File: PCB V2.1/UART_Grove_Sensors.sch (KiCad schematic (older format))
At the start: 0 parts

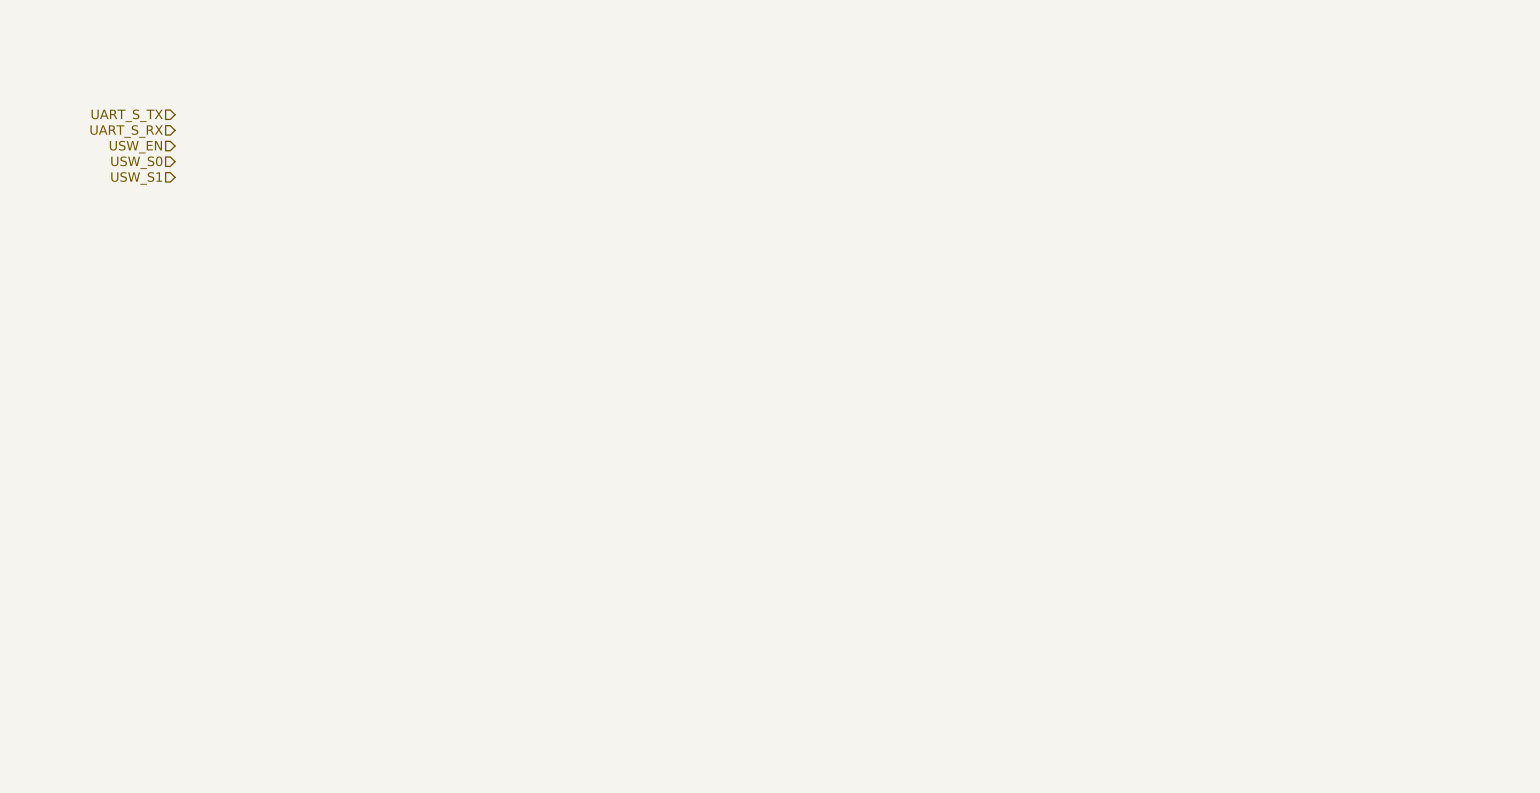
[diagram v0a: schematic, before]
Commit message: SunLeaf Alpha 0.2 and KiCAD Port
SunLeaf rev 2 called Alhpa 0.2 or 0.2a is the main component of this
commit. The entire hardware project has been ported to KiCAD libaries
and all. 0.2a features a revised formfactor, better ESP module, and many
fixes over the original. This version will also be capable of OTA
updates.
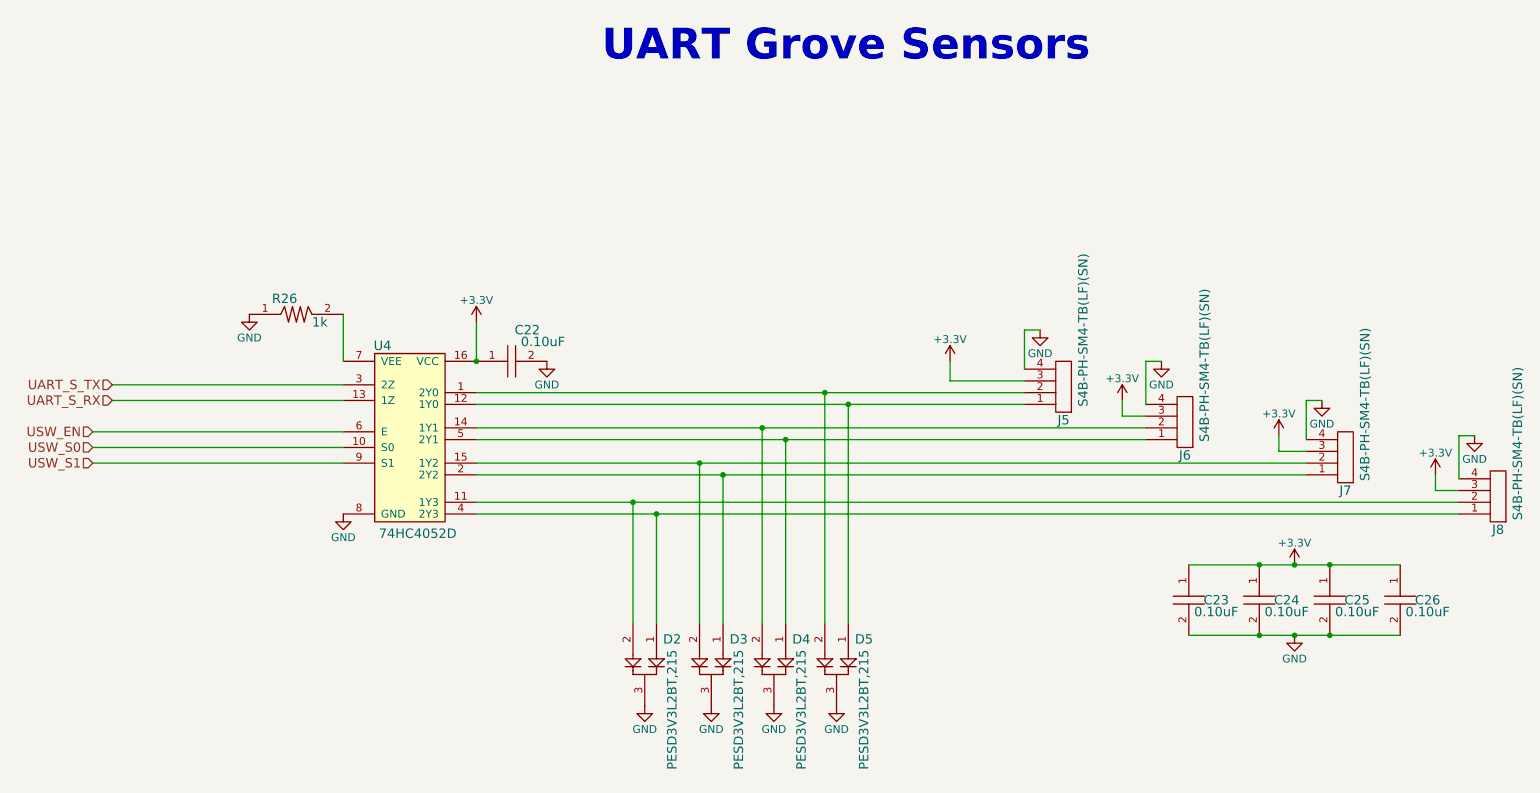
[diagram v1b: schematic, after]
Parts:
- added C22, C23, C24, C25, C26: CL05B104JP5NNNC, PCB_Footprints:C0402, symbol CL05B104JP5NNNC
- added D2, D3, D4, D5: PESD3V3L2BT,215, PCB_Footprints:BAT20JFILM, symbol PESD3V3L2BT,215
- added J5, J6, J7, J8: S4B-PH-SM4-TB(LF)(SN), PCB_Footprints:S4B-PH-SM4-TB(LF)(SN), symbol S4B-PH-SM4-TB(LF)(SN)
- added R26: RC1005F102CS, PCB_Footprints:R0402, symbol RC1005F102CS
- added U4: 74HC4052D, PCB_Footprints:74HC4052D, symbol 74HC4052D
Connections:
- net UART_S_RX: now also U4.13 (1Z)
- net UART_S_TX: now also U4.3 (2Z)
- net USW_EN: now also U4.6 (E)
- net USW_S0: now also U4.10 (S0)
- net USW_S1: now also U4.9 (S1)
- new net: D5.1, J5.1, U4.12 (1Y0)
- new net: D5.2, J5.2, U4.1 (2Y0)
- new net: D2.1, J8.1, U4.4 (2Y3)
- new net: D2.2, J8.2, U4.11 (1Y3)
- new net: R26.2, U4.7 (VEE)
- new net: D4.1, J6.1, U4.5 (2Y1)
- new net: D4.2, J6.2, U4.14 (1Y1)
- new net: D3.1, J7.1, U4.2 (2Y2)
- new net: D3.2, J7.2, U4.15 (1Y2)
- new net +3V3: C22.1, C23.1, C24.1, C25.1, C26.1, J5.3, J6.3, J7.3, J8.3, U4.16 (VCC)
- new net GND: C22.2, C23.2, C24.2, C25.2, C26.2, D2.3, D3.3, D4.3, D5.3, J5.4, J6.4, J7.4, J8.4, R26.1, U4.8 (GND)
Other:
- note added: "UART Grove Sensors"

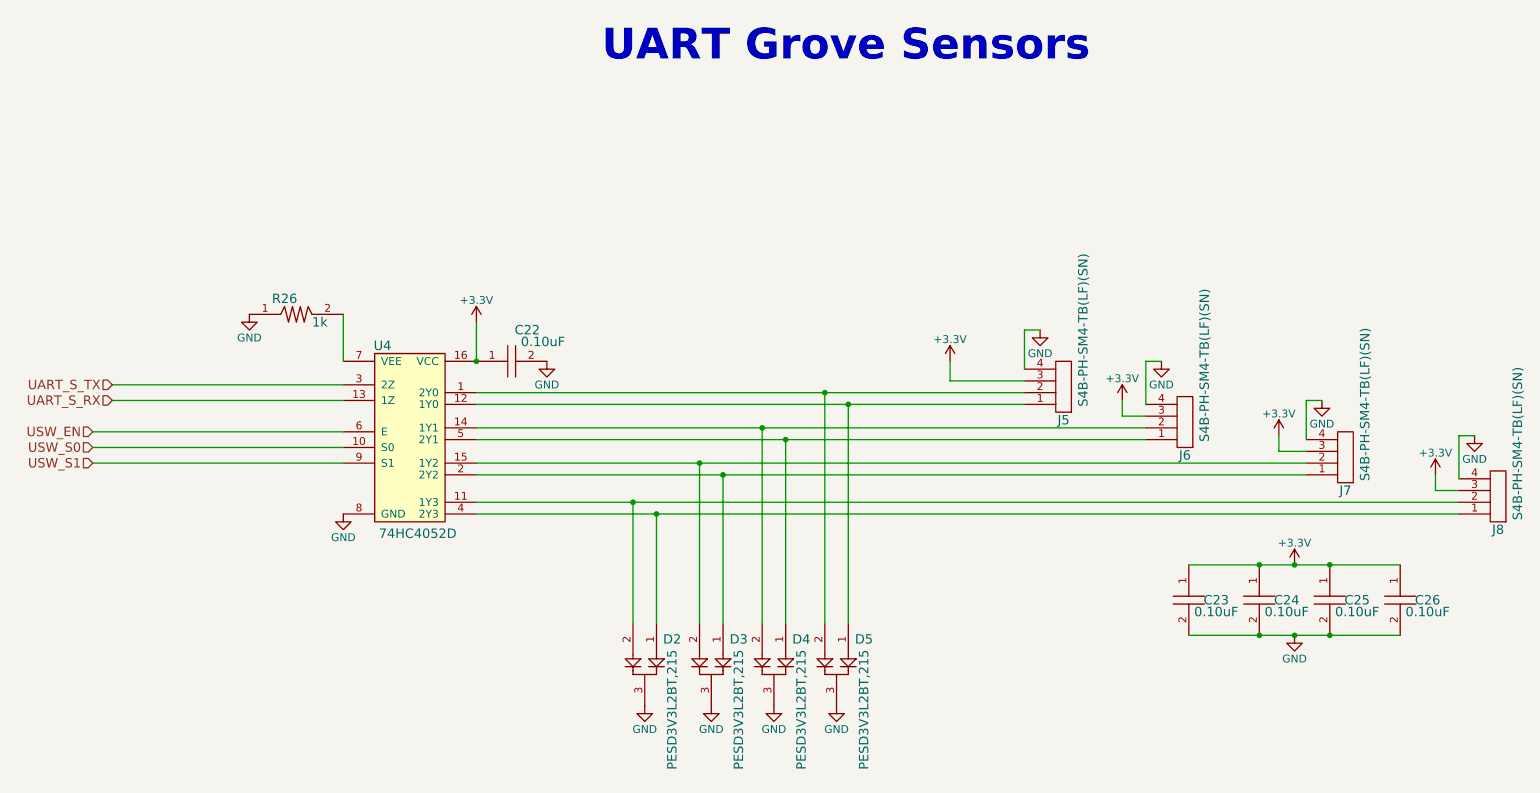
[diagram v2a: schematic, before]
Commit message: Placement
Heavy progress on component placement in KiCAD for SunLEaf V2,
committing to save progress, nightly builds of KiCAD are very crash
prone.
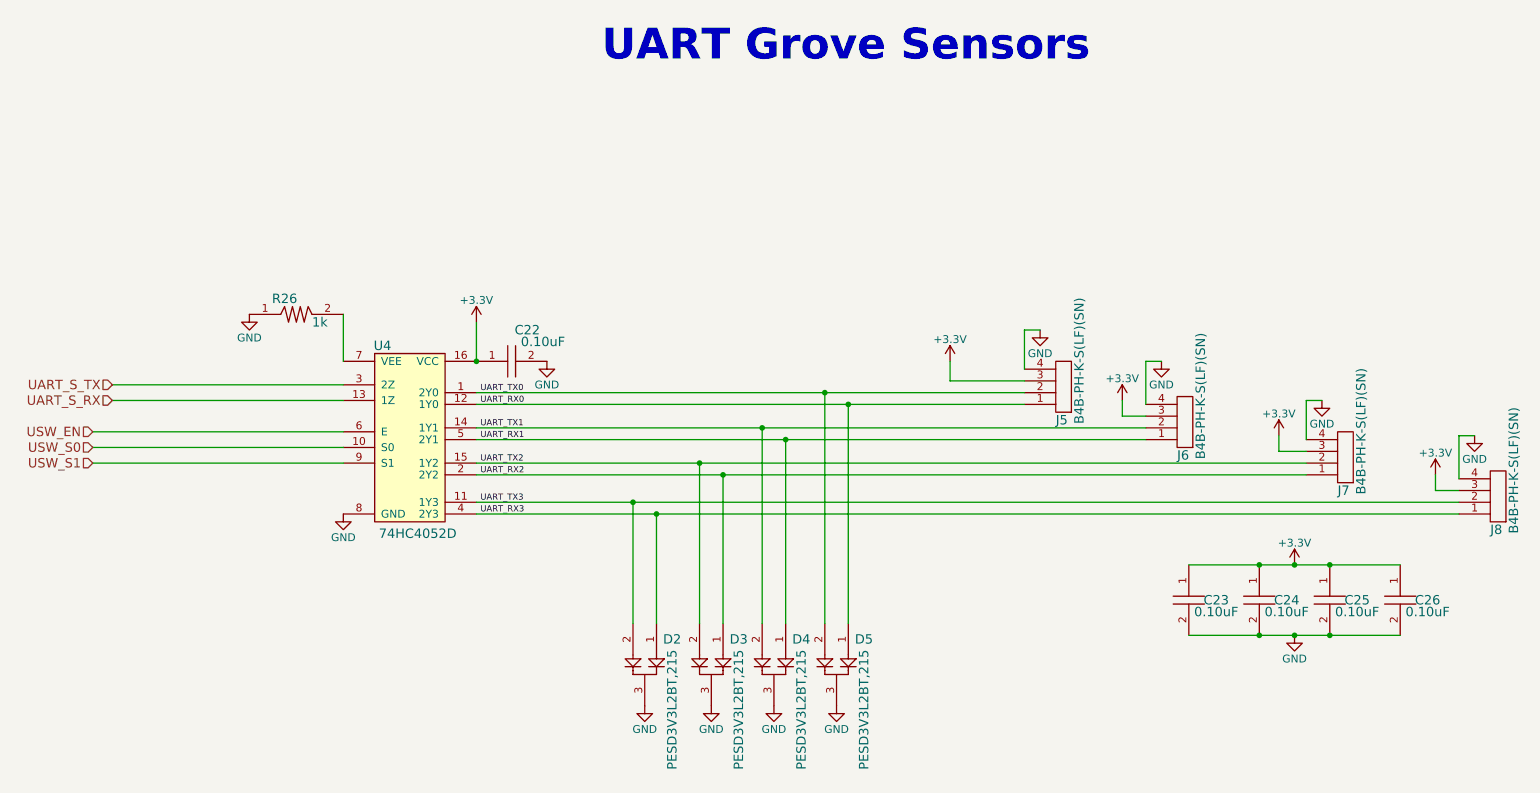
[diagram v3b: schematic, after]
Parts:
- removed J5, J6, J7, J8: S4B-PH-SM4-TB(LF)(SN), PCB_Footprints:S4B-PH-SM4-TB(LF)(SN), symbol S4B-PH-SM4-TB(LF)(SN)
- added J5, J6, J7, J8: B4B-PH-K-S(LF)(SN), PCB_Footprints:B4B-PH-K-S(LF)(SN), symbol B4B-PH-K-S(LF)(SN)
- D2, D3, D4, D5: footprint PCB_Footprints:BAT20JFILM -> PCB_Footprints:PESD3V3L2BT,215
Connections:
- net +3V3: now also J5.3, J6.3, J7.3, J8.3
- net GND: now also J5.4, J6.4, J7.4, J8.4
- net UART_RX0: now reaches D5.1, U4.12 (1Y0)
- net UART_RX0: now also J5.1
- net UART_TX0: now reaches D5.2, U4.1 (2Y0)
- net UART_TX0: now also J5.2
- net UART_RX3: now reaches D2.1, U4.4 (2Y3)
- net UART_RX3: now also J8.1
- net UART_TX3: now reaches D2.2, U4.11 (1Y3)
- net UART_TX3: now also J8.2
- net UART_RX1: now reaches D4.1, U4.5 (2Y1)
- net UART_RX1: now also J6.1
- net UART_TX1: now reaches D4.2, U4.14 (1Y1)
- net UART_TX1: now also J6.2
- net UART_RX2: now reaches D3.1, U4.2 (2Y2)
- net UART_RX2: now also J7.1
- net UART_TX2: now reaches D3.2, U4.15 (1Y2)
- net UART_TX2: now also J7.2

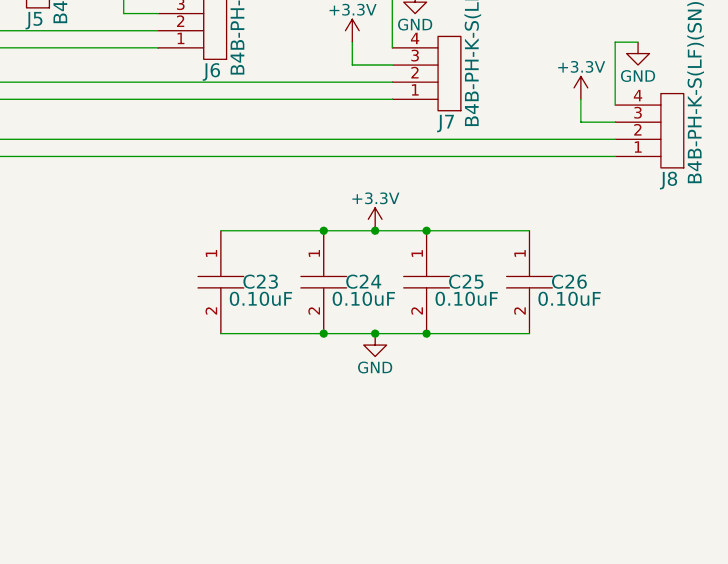
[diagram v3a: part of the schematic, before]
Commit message: Placement progress
Placement is 99% done board is being resized. Next commit TVS diode
pairs will be fliped and the baord further resized.
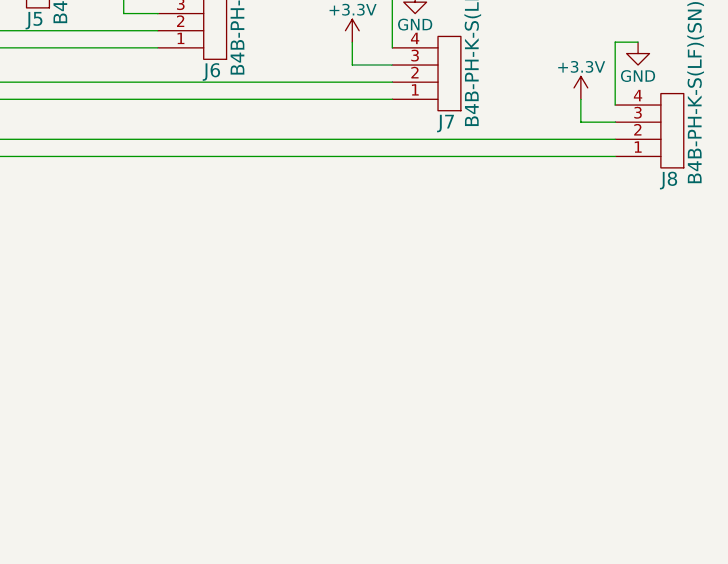
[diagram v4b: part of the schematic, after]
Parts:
- removed C23, C24, C25, C26: CL05B104JP5NNNC, PCB_Footprints:C0402, symbol CL05B104JP5NNNC
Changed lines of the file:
@@
-$EndComp
-$Comp
-L CL05B104JP5NNNC C23
-U 1 1 57D8F945
-P 7925 5275
-F 0 "C23" V 7900 5450 60  0000 C CNN
-F 1 "CL05B104JP5NNNC" H 7975 5125 60  0001 C CNN
-F 2 "PCB_Footprints:C0402" H 8175 5325 60  0001 C CNN
-F 3 "http://www.samsungsem.com/kr/support/product-search/mlcc/__icsFiles/afieldfile/2016/08/18/S_CL05B104JP5NNNC.pdf" H 8175 5325 60  0001 C CNN
-F 4 "$0.00903 @ 5000" H 7825 5525 60  0001 C CNN "Cost"
-F 5 "4 Sept 2016" H 7925 5625 60  0001 C CNN "Date Created"
-F 6 "5 Sept 2016" H 8025 5725 60  0001 C CNN "Date Modified"
-F 7 "Adam Vadala-Roth" H 8125 5825 60  0001 C CNN "Designer"
-F 8 "0.55mm" H 8225 5925 60  0001 C CNN "Height"
-F 9 "Yes" H 8325 6025 60  0001 C CNN "RHoS?"
-F 10 "Samsung Electro-Mechanics America, Inc." H 8425 6125 60  0001 C CNN "MFR"
-F 11 "CL05B104JP5NNNC" H 8525 6225 60  0001 C CNN "MFR#"
-F 12 "SMT/SMD" H 8625 6325 60  0001 C CNN "Mounting"
-F 13 "2" H 8725 6425 60  0001 C CNN "Pint Count#"
-F 14 "Active" H 8825 6525 60  0001 C CNN "Status"
-F 15 "5%" H 8925 6625 60  0001 C CNN "Tolerance"
-F 16 "Ceramic Capacitor 0402" H 9025 6725 60  0001 C CNN "Type"
-F 17 "10V" H 9125 6825 60  0001 C CNN "Voltage"
-F 18 "N/A" H 9225 6925 60  0001 C CNN "Wattage"
-F 19 "0.10uF" V 7975 5450 60  0000 C CNN "Component-Value"
-F 20 "0.10µF 10V Ceramic Capacitor X7R 0402 (1005 Metric) 0.039\" L x 0.020\" W (1.00mm x 0.50mm)" H 9425 7125 60  0001 C CNN "Description"
-	1    7925 5275
-	0    1    1    0
 $EndComp
 $Comp
@@
 $EndComp
 $Comp
-L GND #PWR51
-U 1 1 57D95A00
-P 8600 5475
-F 0 "#PWR51" H 8600 5225 50  0001 C CNN
-F 1 "GND" H 8600 5325 50  0000 C CNN
-F 2 "" H 8600 5475 50  0000 C CNN
-F 3 "" H 8600 5475 50  0000 C CNN
-	1    8600 5475
-	1    0    0    -1
-$EndComp
-$Comp
 L GND #PWR52
 U 1 1 57D95B46
@@
 F 3 "" H 8775 3975 50  0000 C CNN
 	1    8775 3975
-	1    0    0    -1
-$EndComp
-$Comp
-L CL05B104JP5NNNC C24
-U 1 1 57D961FE
-P 8375 5275
-F 0 "C24" V 8350 5450 60  0000 C CNN
-F 1 "CL05B104JP5NNNC" H 8425 5125 60  0001 C CNN
-F 2 "PCB_Footprints:C0402" H 8625 5325 60  0001 C CNN
-F 3 "http://www.samsungsem.com/kr/support/product-search/mlcc/__icsFiles/afieldfile/2016/08/18/S_CL05B104JP5NNNC.pdf" H 8625 5325 60  0001 C CNN
-F 4 "$0.00903 @ 5000" H 8275 5525 60  0001 C CNN "Cost"
-F 5 "4 Sept 2016" H 8375 5625 60  0001 C CNN "Date Created"
-F 6 "5 Sept 2016" H 8475 5725 60  0001 C CNN "Date Modified"
-F 7 "Adam Vadala-Roth" H 8575 5825 60  0001 C CNN "Designer"
-F 8 "0.55mm" H 8675 5925 60  0001 C CNN "Height"
-F 9 "Yes" H 8775 6025 60  0001 C CNN "RHoS?"
-F 10 "Samsung Electro-Mechanics America, Inc." H 8875 6125 60  0001 C CNN "MFR"
-F 11 "CL05B104JP5NNNC" H 8975 6225 60  0001 C CNN "MFR#"
-F 12 "SMT/SMD" H 9075 6325 60  0001 C CNN "Mounting"
-F 13 "2" H 9175 6425 60  0001 C CNN "Pint Count#"
-F 14 "Active" H 9275 6525 60  0001 C CNN "Status"
-F 15 "5%" H 9375 6625 60  0001 C CNN "Tolerance"
-F 16 "Ceramic Capacitor 0402" H 9475 6725 60  0001 C CNN "Type"
-F 17 "10V" H 9575 6825 60  0001 C CNN "Voltage"
-F 18 "N/A" H 9675 6925 60  0001 C CNN "Wattage"
-F 19 "0.10uF" V 8425 5450 60  0000 C CNN "Component-Value"
-F 20 "0.10µF 10V Ceramic Capacitor X7R 0402 (1005 Metric) 0.039\" L x 0.020\" W (1.00mm x 0.50mm)" H 9875 7125 60  0001 C CNN "Description"
-	1    8375 5275
-	0    1    1    0
-$EndComp
-$Comp
-L CL05B104JP5NNNC C25
-U 1 1 57D9626E
-P 8825 5275
-F 0 "C25" V 8800 5450 60  0000 C CNN
-F 1 "CL05B104JP5NNNC" H 8875 5125 60  0001 C CNN
-F 2 "PCB_Footprints:C0402" H 9075 5325 60  0001 C CNN
-F 3 "http://www.samsungsem.com/kr/support/product-search/mlcc/__icsFiles/afieldfile/2016/08/18/S_CL05B104JP5NNNC.pdf" H 9075 5325 60  0001 C CNN
-F 4 "$0.00903 @ 5000" H 8725 5525 60  0001 C CNN "Cost"
-F 5 "4 Sept 2016" H 8825 5625 60  0001 C CNN "Date Created"
-F 6 "5 Sept 2016" H 8925 5725 60  0001 C CNN "Date Modified"
-F 7 "Adam Vadala-Roth" H 9025 5825 60  0001 C CNN "Designer"
-F 8 "0.55mm" H 9125 5925 60  0001 C CNN "Height"
-F 9 "Yes" H 9225 6025 60  0001 C CNN "RHoS?"
-F 10 "Samsung Electro-Mechanics America, Inc." H 9325 6125 60  0001 C CNN "MFR"
-F 11 "CL05B104JP5NNNC" H 9425 6225 60  0001 C CNN "MFR#"
-F 12 "SMT/SMD" H 9525 6325 60  0001 C CNN "Mounting"
-F 13 "2" H 9625 6425 60  0001 C CNN "Pint Count#"
-F 14 "Active" H 9725 6525 60  0001 C CNN "Status"
-F 15 "5%" H 9825 6625 60  0001 C CNN "Tolerance"
-F 16 "Ceramic Capacitor 0402" H 9925 6725 60  0001 C CNN "Type"
-F 17 "10V" H 10025 6825 60  0001 C CNN "Voltage"
-F 18 "N/A" H 10125 6925 60  0001 C CNN "Wattage"
-F 19 "0.10uF" V 8875 5450 60  0000 C CNN "Component-Value"
-F 20 "0.10µF 10V Ceramic Capacitor X7R 0402 (1005 Metric) 0.039\" L x 0.020\" W (1.00mm x 0.50mm)" H 10325 7125 60  0001 C CNN "Description"
-	1    8825 5275
-	0    1    1    0
-$EndComp
-$Comp
-L CL05B104JP5NNNC C26
-U 1 1 57D962E7
-P 9275 5275
-F 0 "C26" V 9250 5450 60  0000 C CNN
-F 1 "CL05B104JP5NNNC" H 9325 5125 60  0001 C CNN
-F 2 "PCB_Footprints:C0402" H 9525 5325 60  0001 C CNN
-F 3 "http://www.samsungsem.com/kr/support/product-search/mlcc/__icsFiles/afieldfile/2016/08/18/S_CL05B104JP5NNNC.pdf" H 9525 5325 60  0001 C CNN
-F 4 "$0.00903 @ 5000" H 9175 5525 60  0001 C CNN "Cost"
-F 5 "4 Sept 2016" H 9275 5625 60  0001 C CNN "Date Created"
-F 6 "5 Sept 2016" H 9375 5725 60  0001 C CNN "Date Modified"
-F 7 "Adam Vadala-Roth" H 9475 5825 60  0001 C CNN "Designer"
-F 8 "0.55mm" H 9575 5925 60  0001 C CNN "Height"
-F 9 "Yes" H 9675 6025 60  0001 C CNN "RHoS?"
-F 10 "Samsung Electro-Mechanics America, Inc." H 9775 6125 60  0001 C CNN "MFR"
-F 11 "CL05B104JP5NNNC" H 9875 6225 60  0001 C CNN "MFR#"
-F 12 "SMT/SMD" H 9975 6325 60  0001 C CNN "Mounting"
-F 13 "2" H 10075 6425 60  0001 C CNN "Pint Count#"
-F 14 "Active" H 10175 6525 60  0001 C CNN "Status"
-F 15 "5%" H 10275 6625 60  0001 C CNN "Tolerance"
-F 16 "Ceramic Capacitor 0402" H 10375 6725 60  0001 C CNN "Type"
-F 17 "10V" H 10475 6825 60  0001 C CNN "Voltage"
-F 18 "N/A" H 10575 6925 60  0001 C CNN "Wattage"
-F 19 "0.10uF" V 9325 5450 60  0000 C CNN "Component-Value"
-F 20 "0.10µF 10V Ceramic Capacitor X7R 0402 (1005 Metric) 0.039\" L x 0.020\" W (1.00mm x 0.50mm)" H 10775 7125 60  0001 C CNN "Description"
-	1    9275 5275
-	0    1    1    0
-$EndComp
-$Comp
-L +3.3V #PWR50
-U 1 1 57D9679F
-P 8600 5025
-F 0 "#PWR50" H 8600 4875 50  0001 C CNN
-F 1 "+3.3V" H 8600 5165 50  0000 C CNN
-F 2 "" H 8600 5025 50  0000 C CNN
-F 3 "" H 8600 5025 50  0000 C CNN
-	1    8600 5025
 	1    0    0    -1
 $EndComp
@@
 	6400 3850 6875 3850
 Wire Wire Line
-	7925 5475 9275 5475
-Wire Wire Line
-	7925 5025 9275 5025
-Connection ~ 8375 5475
-Connection ~ 8600 5475
-Connection ~ 8825 5475
-Connection ~ 8825 5025
-Connection ~ 8375 5025
-Connection ~ 8600 5025
-Wire Wire Line
 	4525 4700 4525 5400
